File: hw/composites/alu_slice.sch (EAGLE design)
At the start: 7 parts, among them CON2 GENERIC-2X10

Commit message: Added tests for addition
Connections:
- net CARRY_OUT: now also OR1.OR; no longer XOR3.XOR
- net SUM: now also XOR3.XOR; no longer OR1.OR
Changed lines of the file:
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@@
 <net name="SUM" class="0">
+<segment>
+<pinref part="SEL2" gate="G$1" pin="I5"/>
+<wire x1="43.18" y1="35.56" x2="40.64" y2="35.56" width="0.1524" layer="91"/>
+<label x="40.64" y="35.56" size="3.81" layer="95" ratio="11" rot="R180" xref="yes"/>
+</segment>
+<segment>
+<pinref part="XOR3" gate="G$1" pin="XOR"/>
+<wire x1="241.3" y1="246.38" x2="294.64" y2="246.38" width="0.1524" layer="91"/>
+<label x="294.64" y="246.38" size="3.81" layer="95" ratio="12" xref="yes"/>
+</segment>
+</net>
+<net name="CARRY_OUT" class="0">
+<segment>
+<pinref part="CON2" gate="G$1" pin="11"/>
+<wire x1="-22.86" y1="-30.48" x2="-27.94" y2="-30.48" width="0.1524" layer="91"/>
+<label x="-27.94" y="-30.48" size="1.27" layer="95" ratio="9" rot="R180" xref="yes"/>
+</segment>
 <segment>
 <pinref part="OR1" gate="G$1" pin="OR"/>
@@
 <label x="294.64" y="208.28" size="3.81" layer="95" ratio="12" xref="yes"/>
 </segment>
-<segment>
-<pinref part="SEL2" gate="G$1" pin="I5"/>
-<wire x1="43.18" y1="35.56" x2="40.64" y2="35.56" width="0.1524" layer="91"/>
-<label x="40.64" y="35.56" size="3.81" layer="95" ratio="11" rot="R180" xref="yes"/>
-</segment>
 </net>
-<net name="CARRY_OUT" class="0">
-<segment>
-<pinref part="XOR3" gate="G$1" pin="XOR"/>
-<wire x1="241.3" y1="246.38" x2="294.64" y2="246.38" width="0.1524" layer="91"/>
-<label x="294.64" y="246.38" size="3.81" layer="95" ratio="12" xref="yes"/>
-</segment>
-<segment>
-<pinref part="CON2" gate="G$1" pin="11"/>
-<wire x1="-22.86" y1="-30.48" x2="-27.94" y2="-30.48" width="0.1524" layer="91"/>
-<label x="-27.94" y="-30.48" size="1.27" layer="95" ratio="9" rot="R180" xref="yes"/>
-</segment>
-</net>

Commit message: Simplified circuit
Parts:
- removed NOT1: NOTVERTICAL, p.peter-gator:NOTVERTICAL
- removed XOR1: XOR, p.peter-gator:XOR
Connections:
- removed net B_INT: XOR1.XOR, XOR2.B
- removed net INVERT: XOR1.B
- removed net N$6: NOT1.A, OR1.B, XOR2.AND
- removed net NAND: NOT1.NOT, SEL2.I8
- new net AND: OR1.B, SEL2.I8, XOR2.AND
- net +5V: no longer NOT1._VP, XOR1._VP
- net B: now also XOR2.B; no longer XOR1.A
- net GND: no longer NOT1._VN, XOR1._VN
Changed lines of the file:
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@@
 </classes>
 <parts>
-<part name="XOR1" library="p.peter-gator" deviceset="XOR" device=""/>
 <part name="XOR2" library="p.peter-gator" deviceset="XOR" device=""/>
 <part name="XOR3" library="p.peter-gator" deviceset="XOR" device=""/>
-<part name="NOT1" library="p.peter-gator" deviceset="NOT" device="VERTICAL" value="NOTVERTICAL"/>
 <part name="OR1" library="p.peter-gator" deviceset="OR" device=""/>
-<part name="P+15" library="supply1" deviceset="+5V" device=""/>
-<part name="GND15" library="supply1" deviceset="GND" device=""/>
 <part name="GND16" library="supply1" deviceset="GND" device=""/>
 <part name="P+16" library="supply1" deviceset="+5V" device=""/>
-<part name="GND17" library="supply1" deviceset="GND" device=""/>
-<part name="P+17" library="supply1" deviceset="+5V" device=""/>
 <part name="P+18" library="supply1" deviceset="+5V" device=""/>
 <part name="P+19" library="supply1" deviceset="+5V" device=""/>
@@
 </plain>
 <instances>
-<instance part="XOR1" gate="G$1" x="-2.54" y="210.82"/>
 <instance part="XOR2" gate="G$1" x="91.44" y="228.6"/>
 <instance part="XOR3" gate="G$1" x="198.12" y="246.38"/>
-<instance part="NOT1" gate="G$1" x="160.02" y="182.88"/>
 <instance part="OR1" gate="G$1" x="271.78" y="208.28"/>
-<instance part="P+15" gate="1" x="-12.7" y="246.38"/>
-<instance part="GND15" gate="1" x="-12.7" y="175.26"/>
 <instance part="GND16" gate="1" x="81.28" y="193.04"/>
 <instance part="P+16" gate="1" x="81.28" y="264.16"/>
-<instance part="GND17" gate="1" x="157.48" y="165.1"/>
-<instance part="P+17" gate="1" x="157.48" y="200.66"/>
 <instance part="P+18" gate="1" x="187.96" y="281.94"/>
 <instance part="P+19" gate="1" x="259.08" y="241.3"/>
@@
 <net name="+5V" class="0">
 <segment>
-<pinref part="XOR1" gate="G$1" pin="_VP"/>
-<pinref part="P+15" gate="1" pin="+5V"/>
-<wire x1="-12.7" y1="243.84" x2="-12.7" y2="241.3" width="0.1524" layer="91"/>
-</segment>
-<segment>
 <pinref part="XOR2" gate="G$1" pin="_VP"/>
 <pinref part="P+16" gate="1" pin="+5V"/>
 <wire x1="81.28" y1="261.62" x2="81.28" y2="259.08" width="0.1524" layer="91"/>
-</segment>
-<segment>
-<pinref part="NOT1" gate="G$1" pin="_VP"/>
-<pinref part="P+17" gate="1" pin="+5V"/>
-<wire x1="157.48" y1="198.12" x2="157.48" y2="195.58" width="0.1524" layer="91"/>
 </segment>
 <segment>
@@
 <net name="GND" class="0">
 <segment>
-<pinref part="XOR1" gate="G$1" pin="_VN"/>
-<pinref part="GND15" gate="1" pin="GND"/>
-<wire x1="-12.7" y1="177.8" x2="-12.7" y2="180.34" width="0.1524" layer="91"/>
-</segment>
-<segment>
 <pinref part="XOR2" gate="G$1" pin="_VN"/>
 <pinref part="GND16" gate="1" pin="GND"/>
 <wire x1="81.28" y1="195.58" x2="81.28" y2="198.12" width="0.1524" layer="91"/>
-</segment>
-<segment>
-<pinref part="NOT1" gate="G$1" pin="_VN"/>
-<pinref part="GND17" gate="1" pin="GND"/>
-<wire x1="157.48" y1="167.64" x2="157.48" y2="170.18" width="0.1524" layer="91"/>
 </segment>
 <segment>
@@
 </segment>
 </net>
-<net name="NAND" class="0">
-<segment>
-<pinref part="NOT1" gate="G$1" pin="NOT"/>
-<wire x1="180.34" y1="182.88" x2="182.88" y2="182.88" width="0.1524" layer="91"/>
-<label x="182.88" y="182.88" size="3.81" layer="95" ratio="12" xref="yes"/>
-</segment>
-<segment>
-<pinref part="SEL2" gate="G$1" pin="I8"/>
-<wire x1="43.18" y1="-25.4" x2="40.64" y2="-25.4" width="0.1524" layer="91"/>
-<label x="40.64" y="-25.4" size="3.81" layer="95" ratio="11" rot="R180" xref="yes"/>
-</segment>
-</net>
-<net name="B_INT" class="0">
-<segment>
-<pinref part="XOR1" gate="G$1" pin="XOR"/>
-<wire x1="40.64" y1="210.82" x2="43.18" y2="210.82" width="0.1524" layer="91"/>
+<net name="B" class="0">
+<segment>
+<wire x1="43.18" y1="210.82" x2="-53.34" y2="228.6" width="0.1524" layer="91"/>
+<label x="-53.34" y="228.6" size="3.81" layer="95" ratio="12" rot="R180" xref="yes"/>
 <pinref part="XOR2" gate="G$1" pin="B"/>
-</segment>
-</net>
-<net name="B" class="0">
-<segment>
-<pinref part="XOR1" gate="G$1" pin="A"/>
-<wire x1="-50.8" y1="228.6" x2="-53.34" y2="228.6" width="0.1524" layer="91"/>
-<label x="-53.34" y="228.6" size="3.81" layer="95" ratio="12" rot="R180" xref="yes"/>
 </segment>
 <segment>
@@
 </segment>
 </net>
-<net name="INVERT" class="0">
-<segment>
-<pinref part="XOR1" gate="G$1" pin="B"/>
-<wire x1="-50.8" y1="193.04" x2="-53.34" y2="193.04" width="0.1524" layer="91"/>
-<label x="-53.34" y="193.04" size="3.81" layer="95" ratio="12" rot="R180" xref="yes"/>
-</segment>
-</net>
 <net name="LEFT_IN" class="0">
 <segment>
@@
 </segment>
 </net>
-<net name="N$6" class="0">
+<net name="AND" class="0">
 <segment>
 <pinref part="OR1" gate="G$1" pin="B"/>
@@
 <pinref part="XOR2" gate="G$1" pin="AND"/>
 <wire x1="177.8" y1="203.2" x2="147.32" y2="203.2" width="0.1524" layer="91"/>
-<pinref part="NOT1" gate="G$1" pin="A"/>
 <wire x1="147.32" y1="203.2" x2="134.62" y2="203.2" width="0.1524" layer="91"/>
 <wire x1="149.86" y1="182.88" x2="147.32" y2="182.88" width="0.1524" layer="91"/>
 <wire x1="147.32" y1="182.88" x2="147.32" y2="203.2" width="0.1524" layer="91"/>
 <junction x="147.32" y="203.2"/>
-</segment>
-</net>
+<label x="149.86" y="182.88" size="3.81" layer="95" ratio="12" xref="yes"/>
+</segment>
+<segment>
+<pinref part="SEL2" gate="G$1" pin="I8"/>
+<wire x1="43.18" y1="-25.4" x2="40.64" y2="-25.4" width="0.1524" layer="91"/>
+<label x="40.64" y="-25.4" size="3.81" layer="95" ratio="11" rot="R180" xref="yes"/>
+</segment>
+</net>

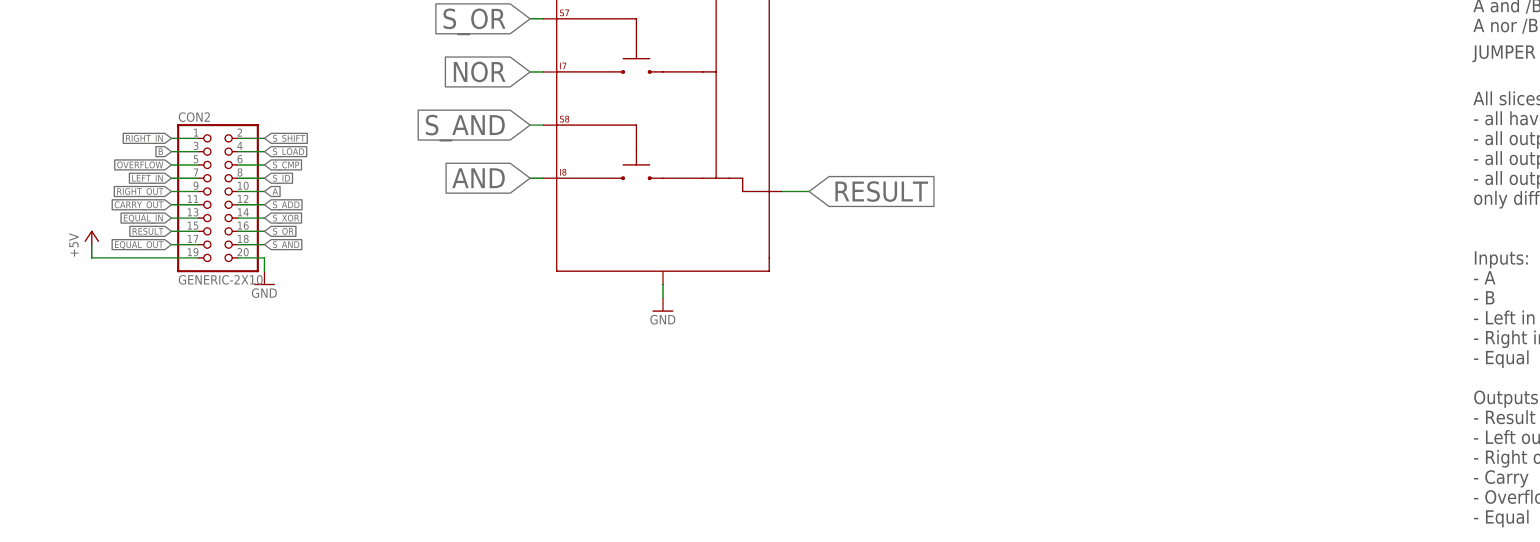
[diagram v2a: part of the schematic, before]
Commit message: Added inversion of output
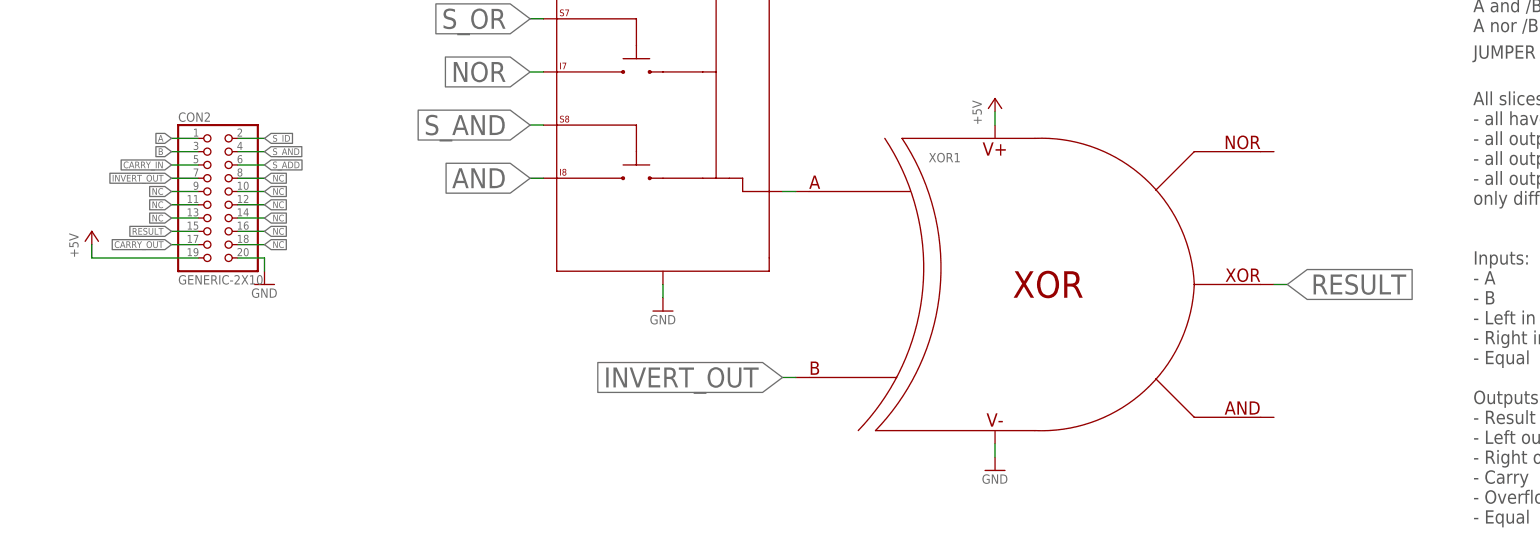
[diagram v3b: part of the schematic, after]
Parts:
- added XOR1: XOR, p.peter-gator:XOR
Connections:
- removed net EQUAL_IN: CON2.13
- removed net EQUAL_OUT: CON2.17
- removed net OVERFLOW: CON2.5
- removed net RIGHT_IN: CON2.1
- removed net RIGHT_OUT: CON2.9
- new net INVERT_OUT: CON2.7, XOR1.B
- new net N$1: SEL2.OUT, XOR1.A
- new net NC: CON2.10, CON2.11, CON2.12, CON2.13, CON2.14, CON2.16, CON2.18, CON2.8, CON2.9
- net +5V: now also XOR1._VP
- net A: now also CON2.1; no longer CON2.10
- net CARRY_IN: now also CON2.5
- net CARRY_OUT: now also CON2.17; no longer CON2.11
- net GND: now also XOR1._VN
- net LEFT_IN: no longer CON2.7
- net RESULT: now also XOR1.XOR; no longer SEL2.OUT
- net S_ADD: now also CON2.6; no longer CON2.12
- net S_AND: now also CON2.4; no longer CON2.18
- net S_CMP: no longer CON2.6
- net S_ID: now also CON2.2; no longer CON2.8
- net S_LOAD: no longer CON2.4
- net S_OR: no longer CON2.16
- net S_SHIFT: no longer CON2.2
- net S_XOR: no longer CON2.14

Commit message: adds substraction
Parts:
- added XOR4: XOR, p.peter-gator:XOR
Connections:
- new net N$2: XOR2.B, XOR4.XOR
- new net SUBTRACT: CON2.9, XOR4.B
- net +5V: now also CON2.2, XOR4._VP; no longer CON2.19
- net B: now also XOR4.A; no longer XOR2.B
- net GND: now also XOR4._VN
- net NC: now also CON2.15; no longer CON2.8, CON2.9
- net RESULT: now also CON2.19; no longer CON2.15
- net S_ADD: now also CON2.8; no longer CON2.6
- net S_AND: now also CON2.6; no longer CON2.4
- net S_ID: now also CON2.4; no longer CON2.2

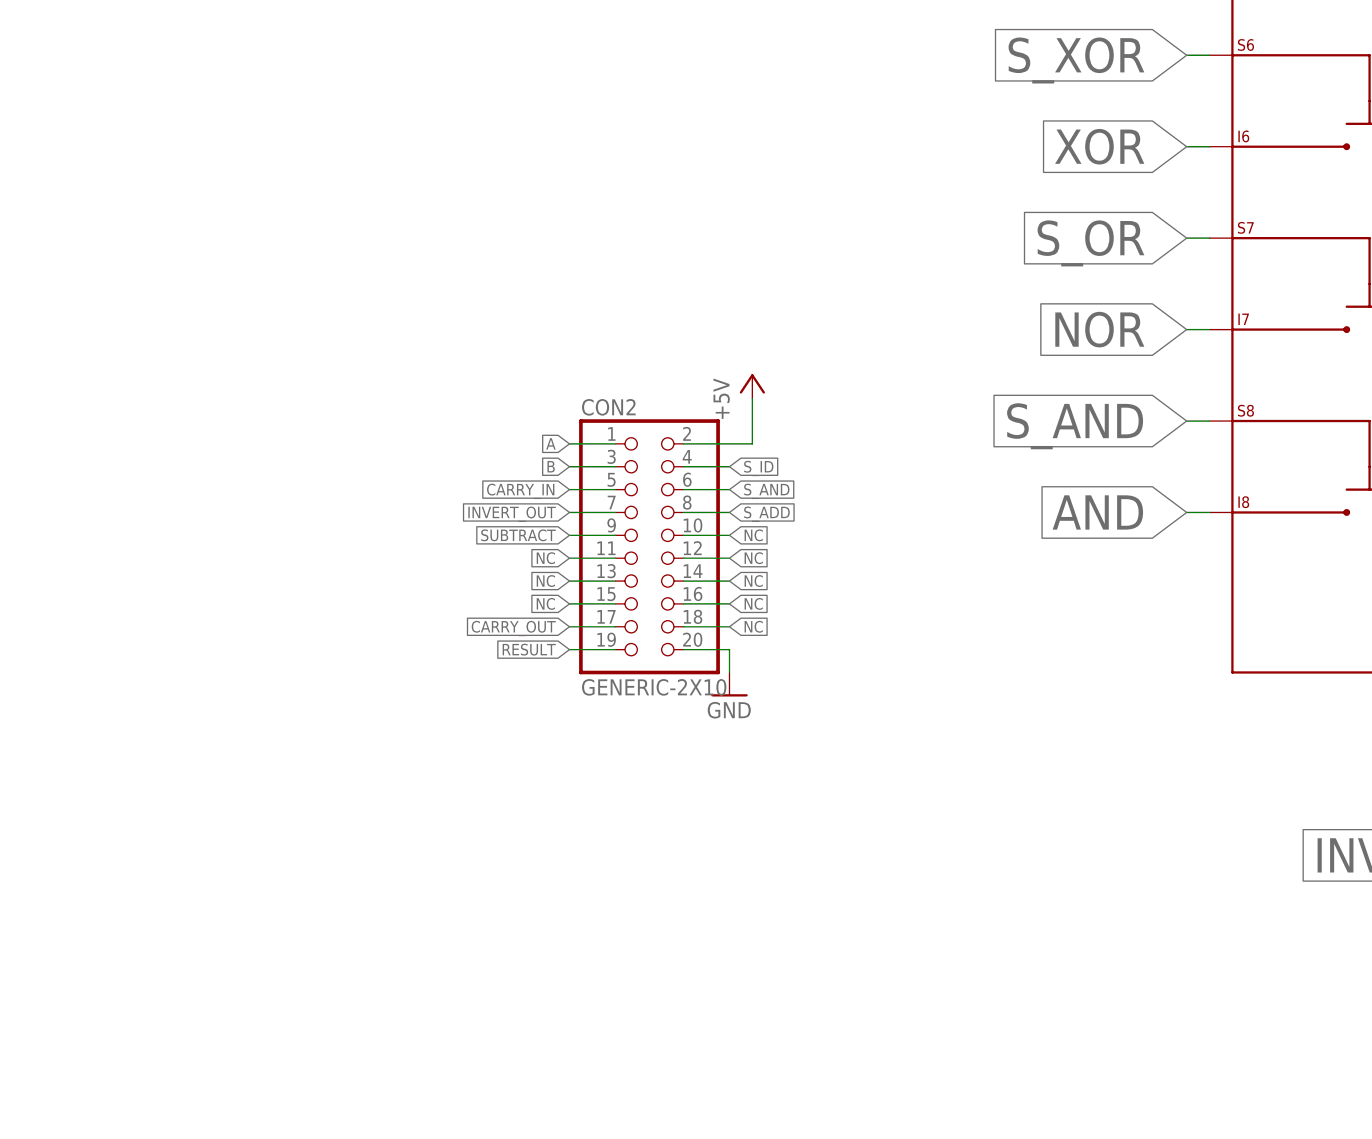
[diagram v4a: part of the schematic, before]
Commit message: adds support for logical OR
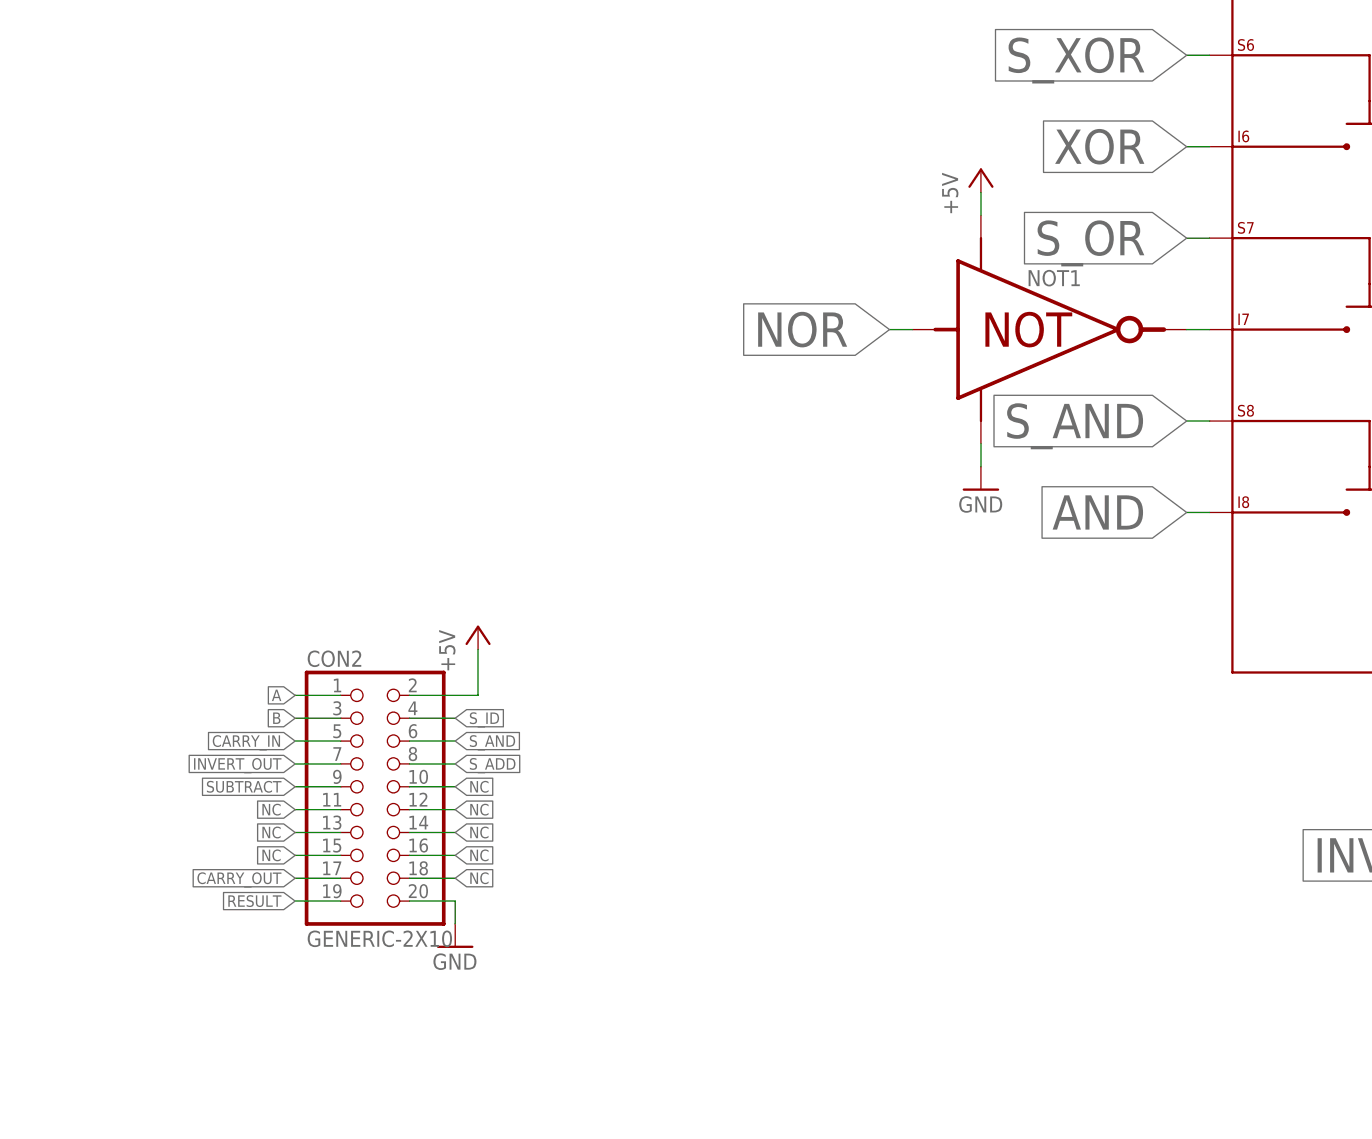
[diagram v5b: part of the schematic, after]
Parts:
- added NOT1: NOTVERTICAL, p.peter-gator:NOTVERTICAL
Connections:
- new net N$3: NOT1.NOT, SEL2.I7
- net +5V: now also NOT1._VP
- net GND: now also NOT1._VN
- net NOR: now also NOT1.A; no longer SEL2.I7
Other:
- moved on the sheet: CON2
